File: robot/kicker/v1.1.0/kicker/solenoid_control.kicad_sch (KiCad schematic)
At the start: 15 parts, among them J3 2157601002, J4 2157601002, Q2 IXGA48N60A3, Q3 IXGA48N60A3, U5 IX4427

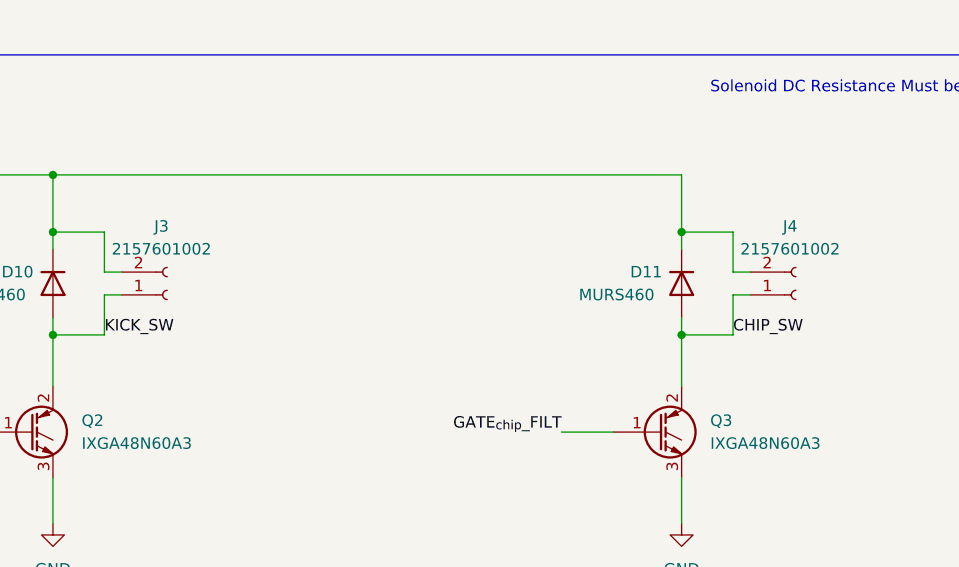
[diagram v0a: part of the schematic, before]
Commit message: address initial issues with v1.0.0
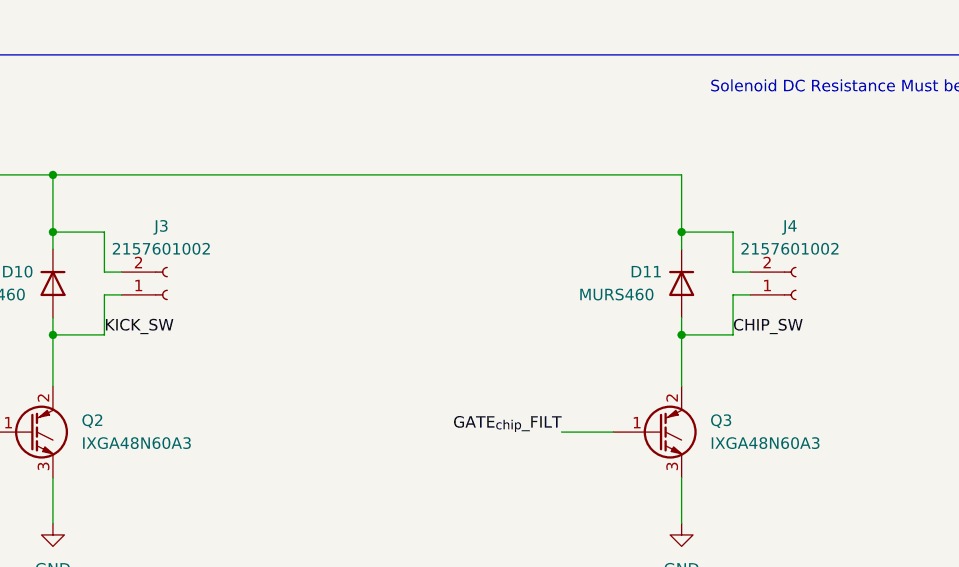
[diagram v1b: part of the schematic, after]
